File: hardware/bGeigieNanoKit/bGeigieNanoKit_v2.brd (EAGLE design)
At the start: 96.2 x 66.7 mm, 37 parts, among them T1 2SC1815

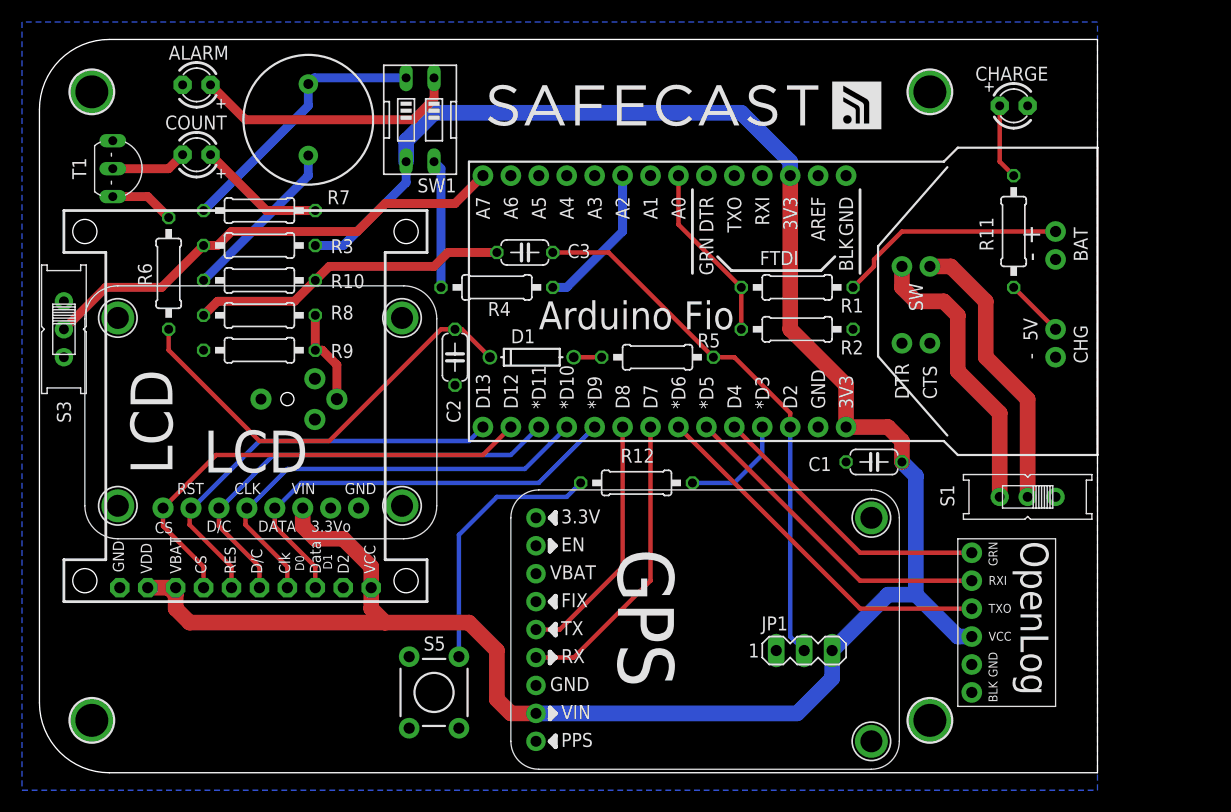
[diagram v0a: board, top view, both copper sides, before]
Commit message: adding v2 version of the board with a single LCD
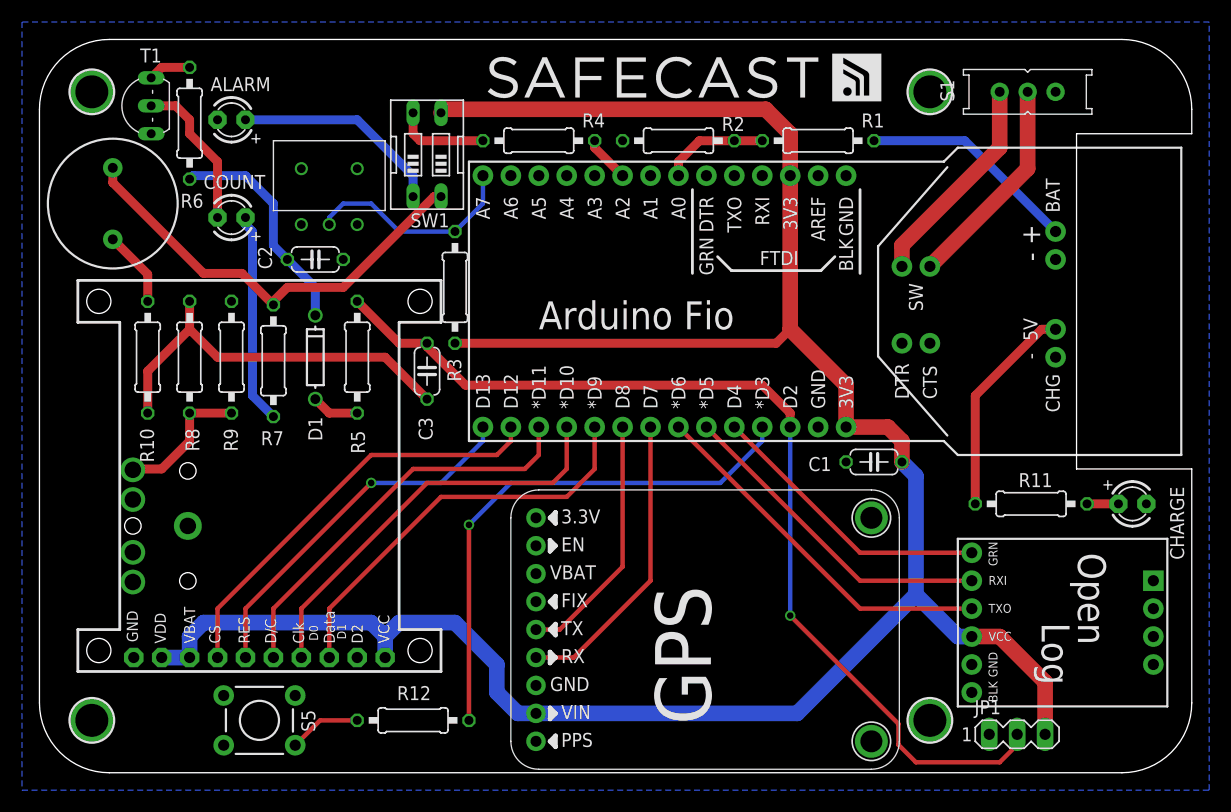
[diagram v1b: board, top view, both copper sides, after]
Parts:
- removed S3: (no value), adafruit:EG1218
- removed U1: (no value), SparkFun:STEREOJACK2.5MM_STEREOJACK2.5MM
- added CN1: (no value), microbuilder:STX3100
- U$1: value OPENLOG_MINITOP -> OPENLOG; device open_hw_sockets:OPENLOG_TOP_MINI -> open_hw_sockets:OPENLOG
- U$4: value LCD -> A12JH; device open_hw_sockets:SSD1306_128X32_SPI_LCD_TOP -> open_hw_sockets:A12AH
- U$5: value SSD1306_128X64_LCD_MIN -> LCD
- moved U$4 40.3 mm to (27.9, 56.5), turned to 180 degrees
- moved CHARGE 37.8 mm to (101.0, 26.0)
- moved S1 36.8 mm to (91.4, 63.5)
- moved R12 29.6 mm to (35.6, 6.35)
- moved R5 27.3 mm to (30.5, 39.4), turned to 270 degrees
- moved R11 24.8 mm to (91.8, 26.0), turned to 180 degrees
- moved JP1 20.8 mm to (90.5, 5.08)
- moved R2 20.3 mm to (59.7, 59.1), turned to 0 degrees
- moved D1 19.7 mm to (26.7, 39.4), turned to 90 degrees
- moved SG1 19.3 mm to (8.26, 53.3)
- moved R3 18.2 mm to (39.4, 45.7), turned to 270 degrees
- moved S5 16.1 mm to (21.6, 6.35), turned to 180 degrees
- moved C2 15.5 mm to (26.7, 48.3), turned to 0 degrees
- moved C3 14.0 mm to (36.8, 38.1), turned to 90 degrees
- moved R4 13.9 mm to (47.0, 59.1)
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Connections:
- net GND: now also CN1.1, U$4.P$3, U$4.P$4, U$4.P$5; no longer S3.S, U$4.JP1$8, U$4.U$2$P$1, U$4.U$3$P$1, U$4.U$4$P$1, U$4.U$5$P$1, U1.RING1, U1.RING2
- net N$1: no longer U$4.JP1$5
- net N$14: now also U$4.P$2; no longer S3.P
- net N$2: no longer U$4.JP1$4
- net N$25: now also CN1.2; no longer U1.TIP
- net N$3: no longer U$4.JP1$3
- net N$4: no longer U$4.JP1$1
- net N$5: no longer U$4.JP1$2
- net VCC: no longer U$4.JP1$6
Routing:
- net N$18: track 49.8 -> 91.1 mm, vias 0 -> 1
- net N$30: track 9.94 -> 48.9 mm, vias 0 -> 1
- net N$14: track 43.9 -> 19.8 mm
- net N$27: track 39.8 -> 20.5 mm
- net N$20: track 24.1 -> 6.58 mm
- net N$21: track 24.6 -> 40.1 mm
- net VIN: track 5.39 -> 19.6 mm
- net VCC: track 204.8 -> 215.8 mm
- net N$15: track 13.5 -> 4.23 mm
- net N$23: track 15.3 -> 6.96 mm
- net N$19: track 11.6 -> 19.1 mm
- net N$22: track 6.88 -> 14.0 mm
- net N$24: track 29.0 -> 36.0 mm
- net N$11: track 16.3 -> 9.68 mm
- net N$13: track 26.1 -> 19.6 mm
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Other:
- board size 96.2 x 66.7 mm -> 104.8 x 66.7 mm
